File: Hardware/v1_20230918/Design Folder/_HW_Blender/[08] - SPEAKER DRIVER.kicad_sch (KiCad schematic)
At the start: 27 parts, among them J801 MHDR_2X1_VERT_1.27MM, J802 MHDR_2X1_VERT_1.27MM, U801 PAM8003DR, U802 PCM1754DBQR

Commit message: Updating Library
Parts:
- C801, C802, C803, C804: symbol _SCHLIB_Blender:CAP_10uF_16V_X5R_C0603 -> _SCHLIB_Blender:CAP_CER_10uF_16V_X5R_C0603
- C805, C806, C808: symbol _SCHLIB_Blender:CAP_2u2F_6V3_X5R_C0201 -> _SCHLIB_Blender:CAP_CER_2u2F_6V3_X5R_C0201
- C807: symbol _SCHLIB_Blender:CAP_1uF_6V3_X5R_C0201 -> _SCHLIB_Blender:CAP_CER_1uF_6V3_X5R_C0201
- U802: Package 16-SSOP (0.154", 3.90mm Width) -> 16-SSOP (3.90mm Width)
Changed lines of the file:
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@@
   )
   (symbol (lib_id "_SCHLIB_Blender:CONN_HEADER_2POS_1ROW_MALE_VERT_1.27MM") (at 495.3 165.1 0) (unit 1)
-    (in_bom yes) (on_board yes) (dnp no) (fields_autoplaced)
+    (in_bom yes) (on_board yes) (dnp no)
     (property "Reference" "J801" (at 500.38 163.83 0)
       (effects (font (size 1.27 1.27)) (justify left))
@@
       (effects (font (size 1.27 1.27)) (justify left) hide)
     )
-    (property "SCH CHECK" "SCH (N/A)" (at 500.38 168.91 0)
+    (property "SCH CHECK" "SCH (N/A)" (at 500.38 171.45 0)
       (effects (font (size 1.27 1.27)) (justify left))
     )
@@
       (effects (font (size 1.27 1.27)) (justify left) hide)
     )
-    (property "Package" "THD-RA-2.54MM" (at 500.38 171.45 0)
+    (property "Package" "THD-RA-2.54MM" (at 500.38 168.91 0)
       (effects (font (size 1.27 1.27)) (justify left))
     )
@@
     )
   )
-  (symbol (lib_id "_SCHLIB_Blender:CAP_2u2F_6V3_X5R_C0201") (at 339.09 198.12 270) (unit 1)
+  (symbol (lib_id "_SCHLIB_Blender:CAP_CER_2u2F_6V3_X5R_C0201") (at 339.09 198.12 270) (unit 1)
     (in_bom yes) (on_board yes) (dnp no)
     (property "Reference" "C806" (at 341.63 199.39 90)
@@
     )
   )
-  (symbol (lib_id "_SCHLIB_Blender:CAP_10uF_16V_X5R_C0603") (at 210.82 195.58 270) (unit 1)
+  (symbol (lib_id "_SCHLIB_Blender:CAP_CER_10uF_16V_X5R_C0603") (at 210.82 195.58 270) (unit 1)
     (in_bom yes) (on_board yes) (dnp no)
     (property "Reference" "C804" (at 213.36 196.85 90)
@@
       (effects (font (size 1.27 1.27)) (justify left) hide)
     )
-    (property "Package" "16-SSOP (0.154\", 3.90mm Width)" (at 241.3 158.75 0)
+    (property "Package" "16-SSOP (3.90mm Width)" (at 241.3 158.75 0)
       (effects (font (size 1.27 1.27)) (justify left))
     )
@@
     )
   )
-  (symbol (lib_id "_SCHLIB_Blender:CAP_10uF_16V_X5R_C0603") (at 312.42 173.99 0) (unit 1)
+  (symbol (lib_id "_SCHLIB_Blender:CAP_CER_10uF_16V_X5R_C0603") (at 312.42 173.99 0) (unit 1)
     (in_bom yes) (on_board yes) (dnp no)
     (property "Reference" "C802" (at 327.66 172.72 0)
@@
   )
   (symbol (lib_id "_SCHLIB_Blender:CONN_HEADER_2POS_1ROW_MALE_VERT_1.27MM") (at 495.3 177.8 0) (unit 1)
-    (in_bom yes) (on_board yes) (dnp no) (fields_autoplaced)
+    (in_bom yes) (on_board yes) (dnp no)
     (property "Reference" "J802" (at 500.38 176.53 0)
       (effects (font (size 1.27 1.27)) (justify left))
@@
       (effects (font (size 1.27 1.27)) (justify left) hide)
     )
-    (property "SCH CHECK" "SCH (N/A)" (at 500.38 181.61 0)
+    (property "SCH CHECK" "SCH (N/A)" (at 500.38 184.15 0)
       (effects (font (size 1.27 1.27)) (justify left))
     )
@@
       (effects (font (size 1.27 1.27)) (justify left) hide)
     )
-    (property "Package" "THD-RA-2.54MM" (at 500.38 184.15 0)
+    (property "Package" "THD-RA-2.54MM" (at 500.38 181.61 0)
       (effects (font (size 1.27 1.27)) (justify left))
     )
@@
     )
   )
-  (symbol (lib_id "_SCHLIB_Blender:CAP_2u2F_6V3_X5R_C0201") (at 308.61 198.12 270) (unit 1)
+  (symbol (lib_id "_SCHLIB_Blender:CAP_CER_2u2F_6V3_X5R_C0201") (at 308.61 198.12 270) (unit 1)
     (in_bom yes) (on_board yes) (dnp no)
     (property "Reference" "C805" (at 311.15 199.39 90)
@@
     )
   )
-  (symbol (lib_id "_SCHLIB_Blender:CAP_2u2F_6V3_X5R_C0201") (at 388.62 198.12 270) (unit 1)
+  (symbol (lib_id "_SCHLIB_Blender:CAP_CER_2u2F_6V3_X5R_C0201") (at 388.62 198.12 270) (unit 1)
     (in_bom yes) (on_board yes) (dnp no)
     (property "Reference" "C808" (at 391.16 199.39 90)
@@
     )
   )
-  (symbol (lib_id "_SCHLIB_Blender:CAP_10uF_16V_X5R_C0603") (at 191.77 195.58 270) (unit 1)
+  (symbol (lib_id "_SCHLIB_Blender:CAP_CER_10uF_16V_X5R_C0603") (at 191.77 195.58 270) (unit 1)
     (in_bom yes) (on_board yes) (dnp no)
     (property "Reference" "C803" (at 194.31 196.85 90)
@@
     )
   )
-  (symbol (lib_id "_SCHLIB_Blender:CAP_1uF_6V3_X5R_C0201") (at 368.3 198.12 270) (unit 1)
+  (symbol (lib_id "_SCHLIB_Blender:CAP_CER_1uF_6V3_X5R_C0201") (at 368.3 198.12 270) (unit 1)
     (in_bom yes) (on_board yes) (dnp no)
     (property "Reference" "C807" (at 370.84 199.39 90)
@@
     )
   )
-  (symbol (lib_id "_SCHLIB_Blender:CAP_10uF_16V_X5R_C0603") (at 312.42 165.1 0) (unit 1)
+  (symbol (lib_id "_SCHLIB_Blender:CAP_CER_10uF_16V_X5R_C0603") (at 312.42 165.1 0) (unit 1)
     (in_bom yes) (on_board yes) (dnp no)
     (property "Reference" "C801" (at 327.66 163.83 0)

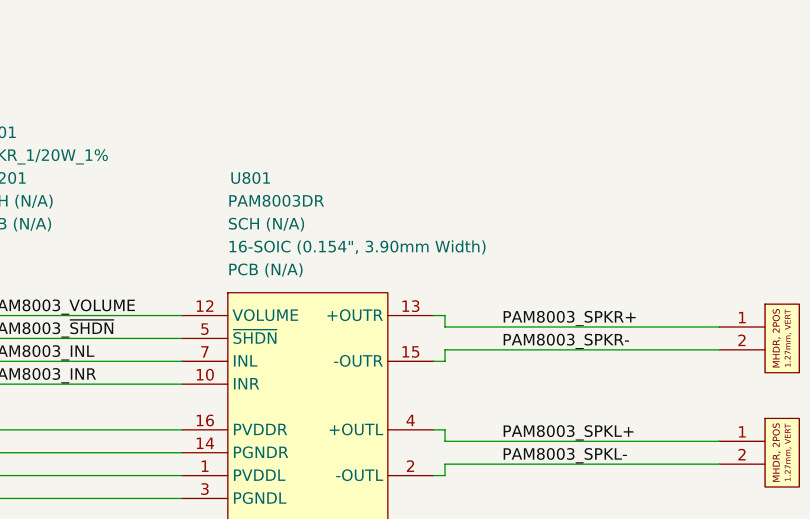
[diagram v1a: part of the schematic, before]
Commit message: Updating 3D components
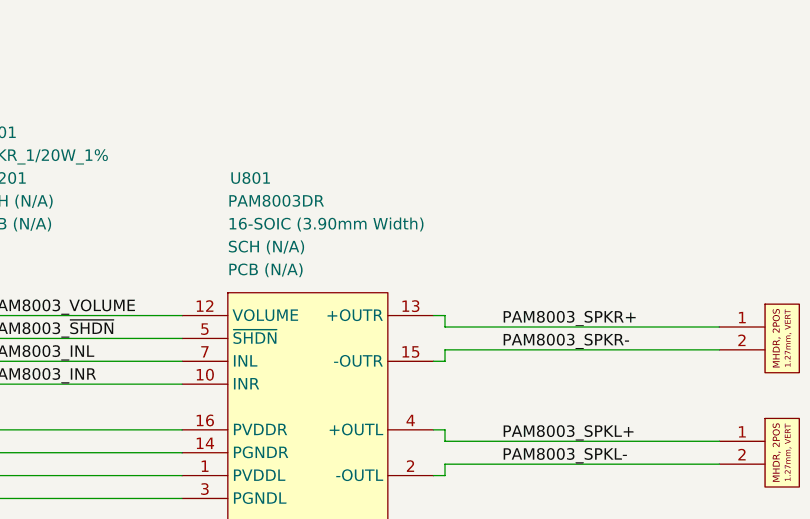
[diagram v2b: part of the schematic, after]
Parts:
- U801: footprint Package_SO:SOP-16_3.9x9.9mm_P1.27mm -> _PCBLIB_Blender:SOP-16_3.9x9.9mm_P1.27mm; Package 16-SOIC (0.154", 3.90mm Width) -> 16-SOIC (3.90mm Width)
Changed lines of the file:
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@@
       (effects (font (size 1.27 1.27)) (justify left))
     )
-    (property "Footprint" "Package_SO:SOP-16_3.9x9.9mm_P1.27mm" (at 438.15 148.59 0)
+    (property "Footprint" "_PCBLIB_Blender:SOP-16_3.9x9.9mm_P1.27mm" (at 438.15 148.59 0)
       (effects (font (size 1.27 1.27)) (justify left) hide)
     )
@@
       (effects (font (size 1.27 1.27)) (justify left) hide)
     )
-    (property "SCH CHECK" "SCH (N/A)" (at 435.61 156.21 0)
+    (property "SCH CHECK" "SCH (N/A)" (at 435.61 158.75 0)
       (effects (font (size 1.27 1.27)) (justify left))
     )
-    (property "Package" "16-SOIC (0.154\", 3.90mm Width)" (at 435.61 158.75 0)
+    (property "Package" "16-SOIC (3.90mm Width)" (at 435.61 156.21 0)
       (effects (font (size 1.27 1.27)) (justify left))
     )
